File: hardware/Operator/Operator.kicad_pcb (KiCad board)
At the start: 2 copper layers, 53.8 x 54.2 mm, 11 parts, among them J1 RJ45, J2 Screw_Terminal_01x02, J3 Conn_01x06_Male, U1 DS89C21

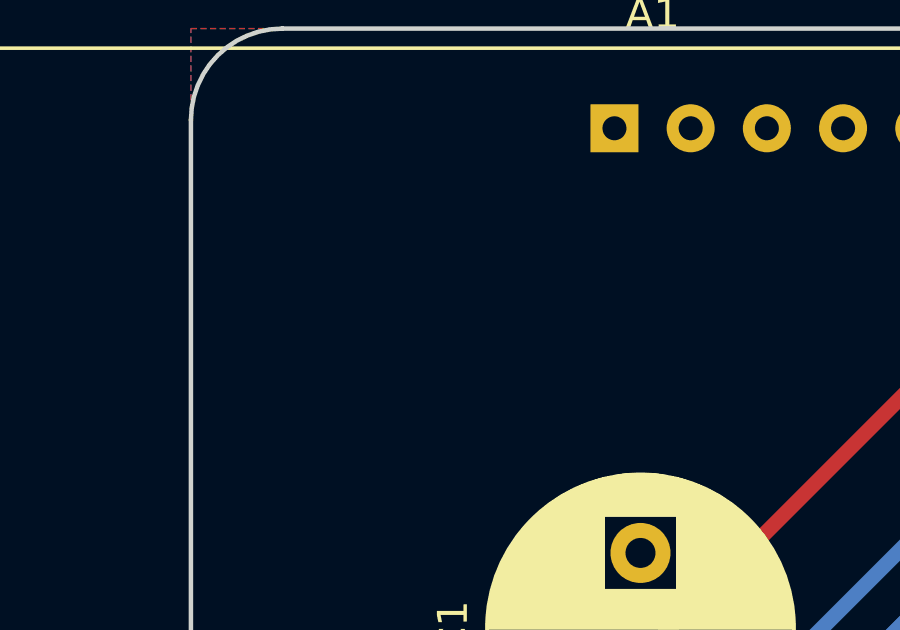
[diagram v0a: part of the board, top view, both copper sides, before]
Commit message: Created silk screen
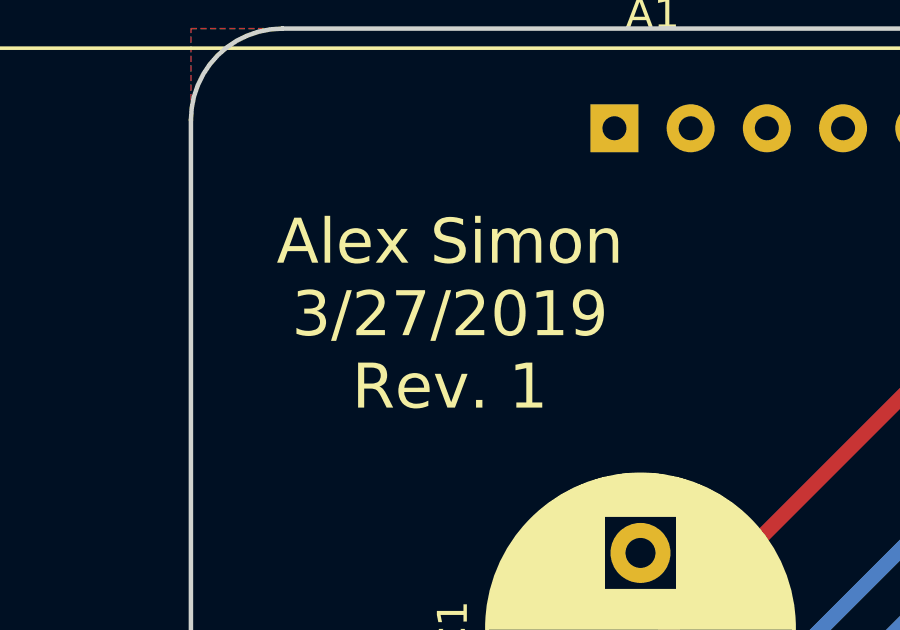
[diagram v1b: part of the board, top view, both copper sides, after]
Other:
- board text added: "Alex Simon 3/27/2019 Rev. 1"
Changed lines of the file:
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@@
   (general
     (thickness 1.6)
-    (drawings 8)
+    (drawings 9)
     (tracks 95)
     (zones 0)
@@
     )
   )
+  (gr_text "Alex Simon\n3/27/2019\nRev. 1" (at 141.986 59.817) (layer F.SilkS)
+    (effects (font (size 1.5 1.5) (thickness 0.3)))
+  )
   (gr_arc (start 184.15 53.34) (end 187.198 53.34) (angle -90) (layer Edge.Cuts) (width 0.15))

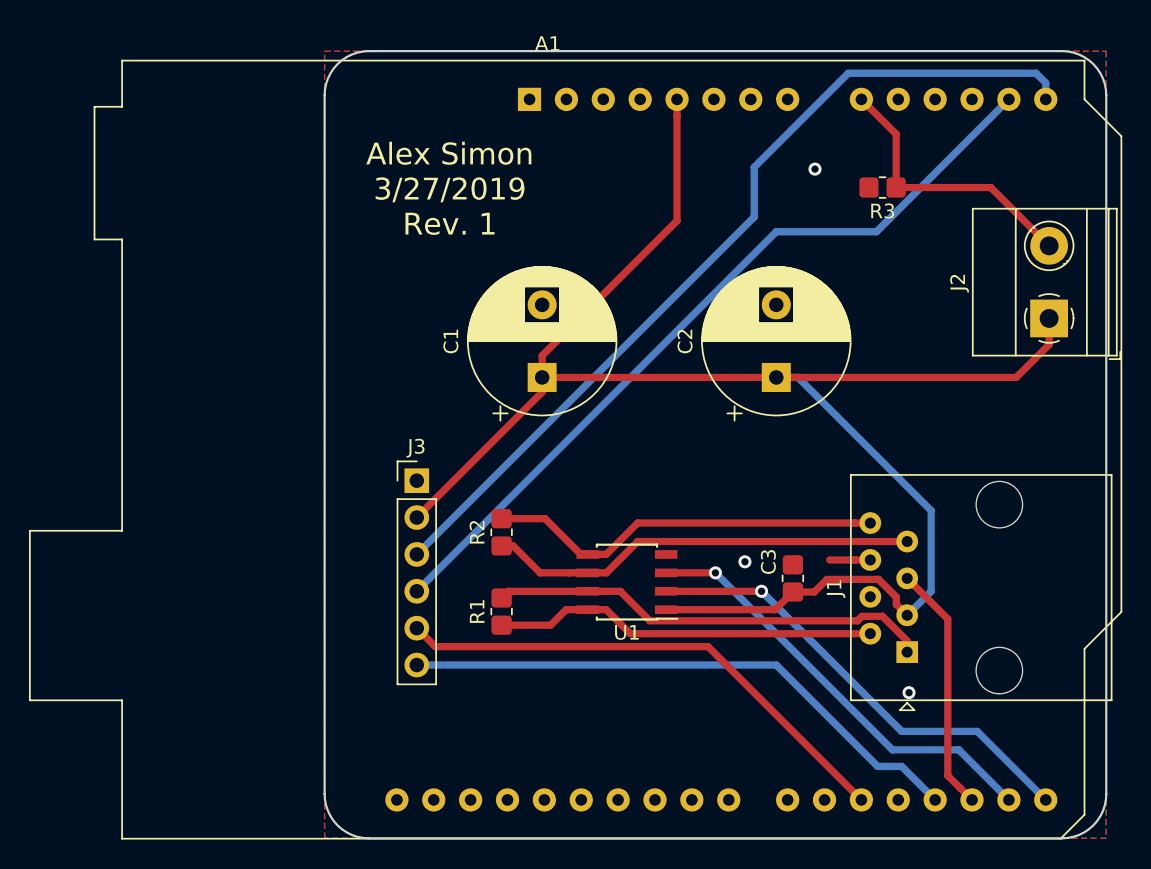
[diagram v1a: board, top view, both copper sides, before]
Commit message: Updated footprint size, put arduino on opposite side of board.
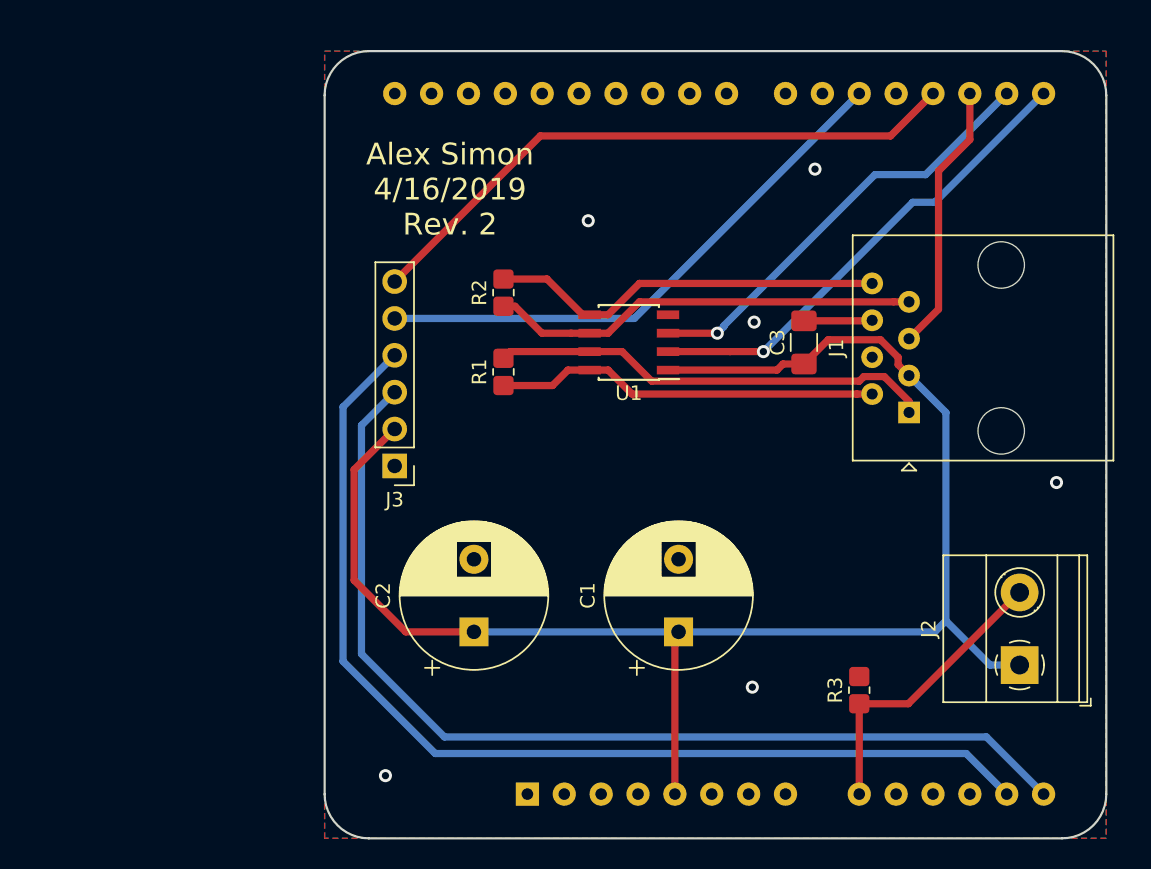
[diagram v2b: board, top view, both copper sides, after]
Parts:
- A1: moved to B.Cu
- C3: value 2.2nF -> 2.2uF; footprint Capacitor_SMD:C_0805_2012Metric_Pad1.33x1.40mm_HandSolder -> Capacitor_SMD:C_1206_3216Metric_Pad1.42x1.75mm_HandSolder
- moved A1 47.9 mm to (147.3, 101.5)
- moved R3 34.7 mm to (170.2, 94.3), turned to 90 degrees
- moved C2 27.2 mm to (143.6, 90.3)
- moved J2 24.0 mm to (181.2, 92.6)
- moved C1 19.9 mm to (157.7, 90.3)
- moved J1 16.5 mm to (173.6, 75.2)
- moved R1 16.5 mm to (145.7, 72.4)
- moved R2 16.5 mm to (145.7, 66.9)
- moved U1 16.5 mm to (154.3, 70.4)
- moved C3 16.3 mm to (166.4, 70.4)
- moved J3 1.83 mm to (138.2, 78.9), turned to 180 degrees
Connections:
- A1 pad 1: Net-(A1-Pad1) -> (no net)
- A1 pad 10: Net-(A1-Pad10) -> (no net)
- A1 pad 11: Net-(A1-Pad11) -> (no net)
- A1 pad 12: Net-(A1-Pad12) -> (no net)
- A1 pad 19: Net-(A1-Pad19) -> (no net)
- A1 pad 2: Net-(A1-Pad2) -> (no net)
- A1 pad 21: Net-(A1-Pad21) -> (no net)
- A1 pad 22: Net-(A1-Pad22) -> (no net)
- A1 pad 23: Net-(A1-Pad23) -> (no net)
- A1 pad 24: Net-(A1-Pad24) -> (no net)
- A1 pad 25: Net-(A1-Pad25) -> (no net)
- A1 pad 26: Net-(A1-Pad26) -> (no net)
- A1 pad 27: Net-(A1-Pad27) -> (no net)
- A1 pad 28: Net-(A1-Pad28) -> (no net)
- A1 pad 3: Net-(A1-Pad3) -> (no net)
- A1 pad 30: Net-(A1-Pad30) -> (no net)
- A1 pad 31: Net-(A1-Pad31) -> (no net)
- A1 pad 32: Net-(A1-Pad32) -> (no net)
- A1 pad 4: Net-(A1-Pad4) -> (no net)
- A1 pad 8: Net-(A1-Pad8) -> (no net)
- J1 pad 4: Net-(J1-Pad4) -> (no net)
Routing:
- net /A4: track 54.8 -> 72.1 mm
- net /A5: track 60.5 -> 70.0 mm
- net /5v: track 115.0 -> 108.5 mm
- net /D5: track 35.5 -> 38.4 mm
- net /D3: track 39.6 -> 42.4 mm
- net /GND: track 2.79 -> 4.71 mm, vias 3 -> 6
- net /TransEnable_TTL: track 17.1 -> 18.6 mm
- net /A0: track 19.3 -> 20.4 mm
- net /USART_RX: track 32.1 -> 33.2 mm
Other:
- board text added: "Alex Simon 4/16/2019 Rev. 2"
- board text removed: "Alex Simon 3/27/2019 Rev. 1"

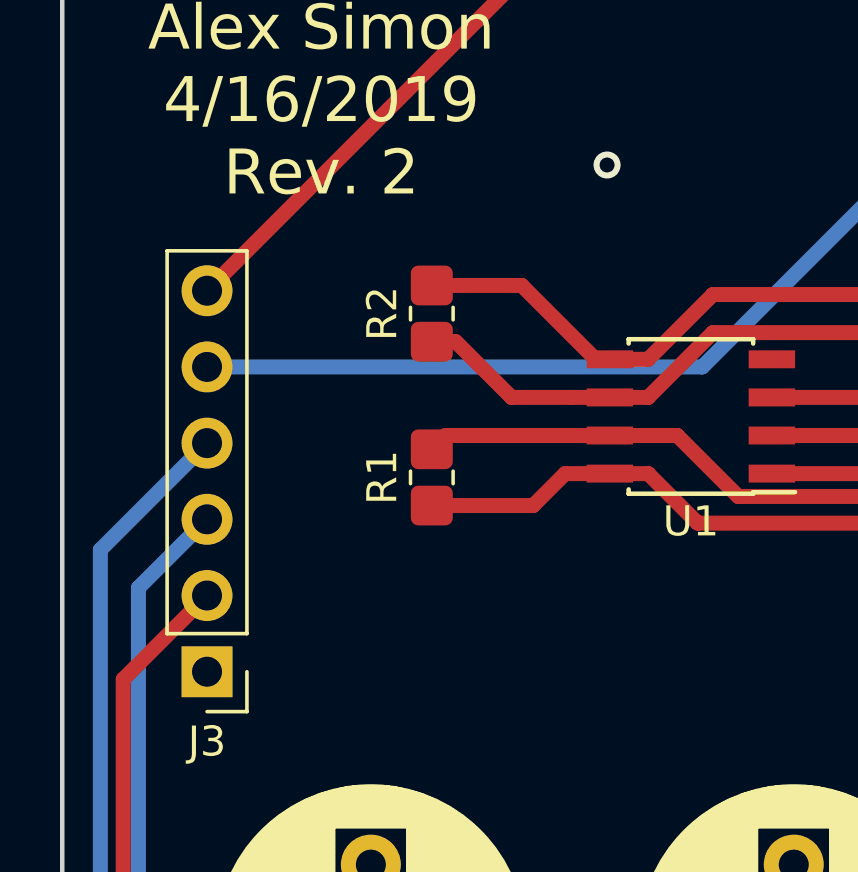
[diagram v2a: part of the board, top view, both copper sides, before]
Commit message: Added RS485 Bias resistors
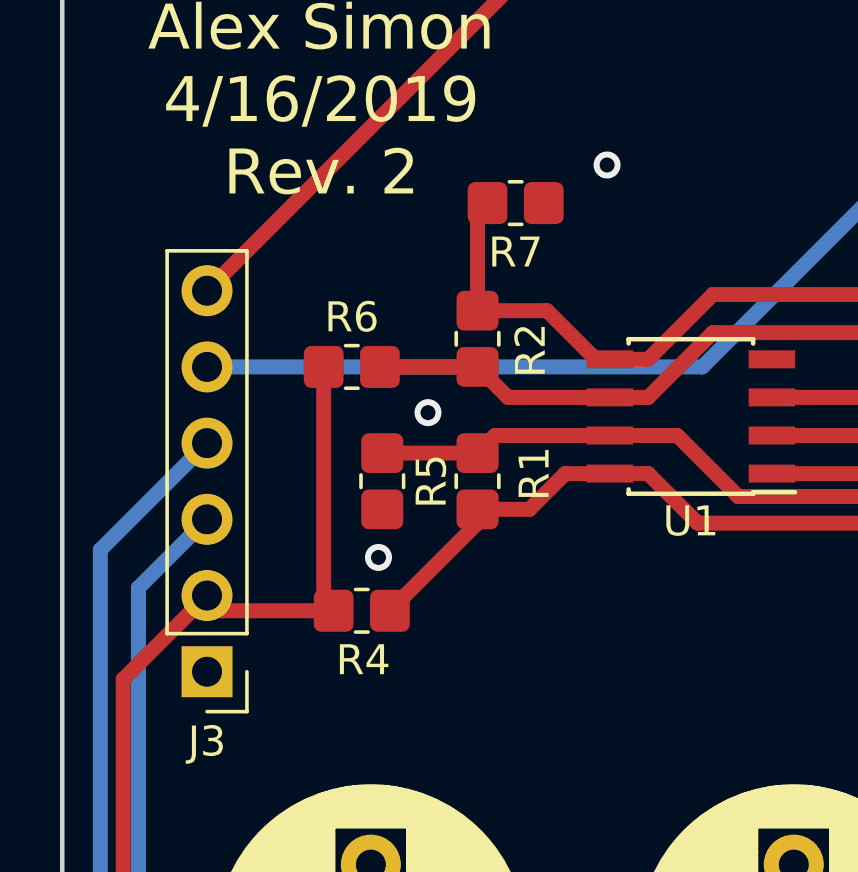
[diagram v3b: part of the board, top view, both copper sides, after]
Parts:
- added R4: 680, Resistor_SMD:R_0805_2012Metric_Pad1.33x1.40mm_HandSolder, F.Cu at (143.3, 76.8)
- added R5: 680, Resistor_SMD:R_0805_2012Metric_Pad1.33x1.40mm_HandSolder, F.Cu at (144.0, 72.5)
- added R6: 680, Resistor_SMD:R_0805_2012Metric_Pad1.33x1.40mm_HandSolder, F.Cu at (143.0, 68.7)
- added R7: 680, Resistor_SMD:R_0805_2012Metric_Pad1.33x1.40mm_HandSolder, F.Cu at (148.5, 63.2)
- moved R2 1.74 mm to (147.2, 67.8)
- moved R1 1.53 mm to (147.2, 72.5)
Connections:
- A1 pad 1: (no net) -> Net-(A1-Pad1)
- A1 pad 10: (no net) -> Net-(A1-Pad10)
- A1 pad 11: (no net) -> Net-(A1-Pad11)
- A1 pad 12: (no net) -> Net-(A1-Pad12)
- A1 pad 19: (no net) -> Net-(A1-Pad19)
- A1 pad 2: (no net) -> Net-(A1-Pad2)
- A1 pad 21: (no net) -> Net-(A1-Pad21)
- A1 pad 22: (no net) -> Net-(A1-Pad22)
- A1 pad 23: (no net) -> Net-(A1-Pad23)
- A1 pad 24: (no net) -> Net-(A1-Pad24)
- A1 pad 25: (no net) -> Net-(A1-Pad25)
- A1 pad 26: (no net) -> Net-(A1-Pad26)
- A1 pad 27: (no net) -> Net-(A1-Pad27)
- A1 pad 28: (no net) -> Net-(A1-Pad28)
- A1 pad 3: (no net) -> Net-(A1-Pad3)
- A1 pad 30: (no net) -> Net-(A1-Pad30)
- A1 pad 31: (no net) -> Net-(A1-Pad31)
- A1 pad 32: (no net) -> Net-(A1-Pad32)
- A1 pad 4: (no net) -> Net-(A1-Pad4)
- A1 pad 8: (no net) -> Net-(A1-Pad8)
- J1 pad 4: (no net) -> Net-(J1-Pad4)
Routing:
- net /5v: track 108.5 -> 121.2 mm
- net /+RX: track 26.5 -> 29.6 mm
- net /-TX: track 27.3 -> 29.2 mm
- net /-RX: track 30.6 -> 32.3 mm
- net /+Tx: track 29.6 -> 31.0 mm
- net /GND: vias 6 -> 8

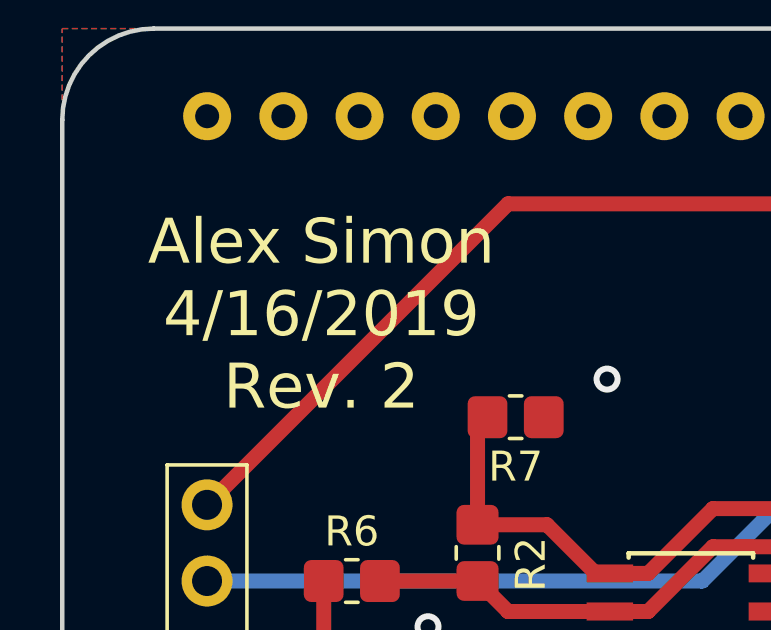
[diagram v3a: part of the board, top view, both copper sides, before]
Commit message: Updated silk screen
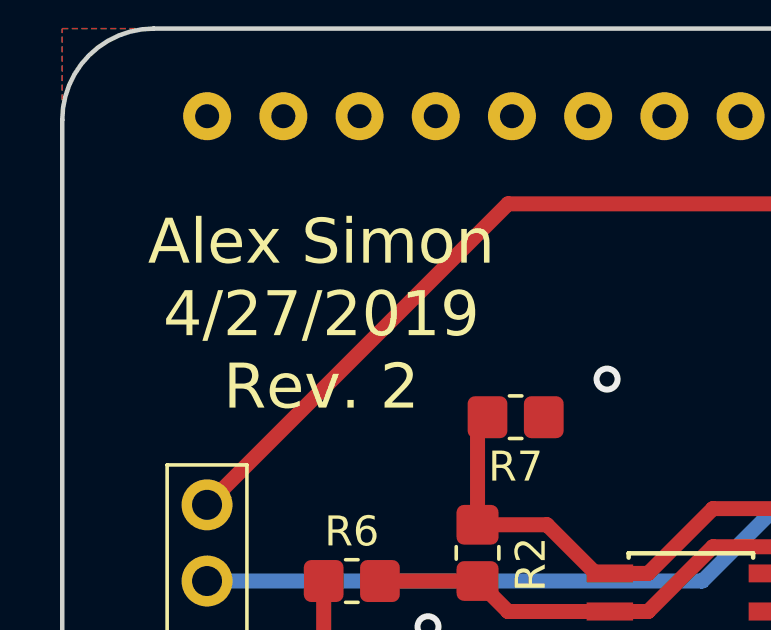
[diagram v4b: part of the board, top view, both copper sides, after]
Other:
- board text added: "Alex Simon 4/27/2019 Rev. 2"
- board text removed: "Alex Simon 4/16/2019 Rev. 2"
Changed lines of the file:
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@@
     )
   )
-  (gr_text "Alex Simon\n4/16/2019\nRev. 2" (at 141.986 59.817) (layer F.SilkS)
+  (gr_text "Alex Simon\n4/27/2019\nRev. 2" (at 141.986 59.817) (layer F.SilkS)
     (effects (font (size 1.5 1.5) (thickness 0.3)))
   )

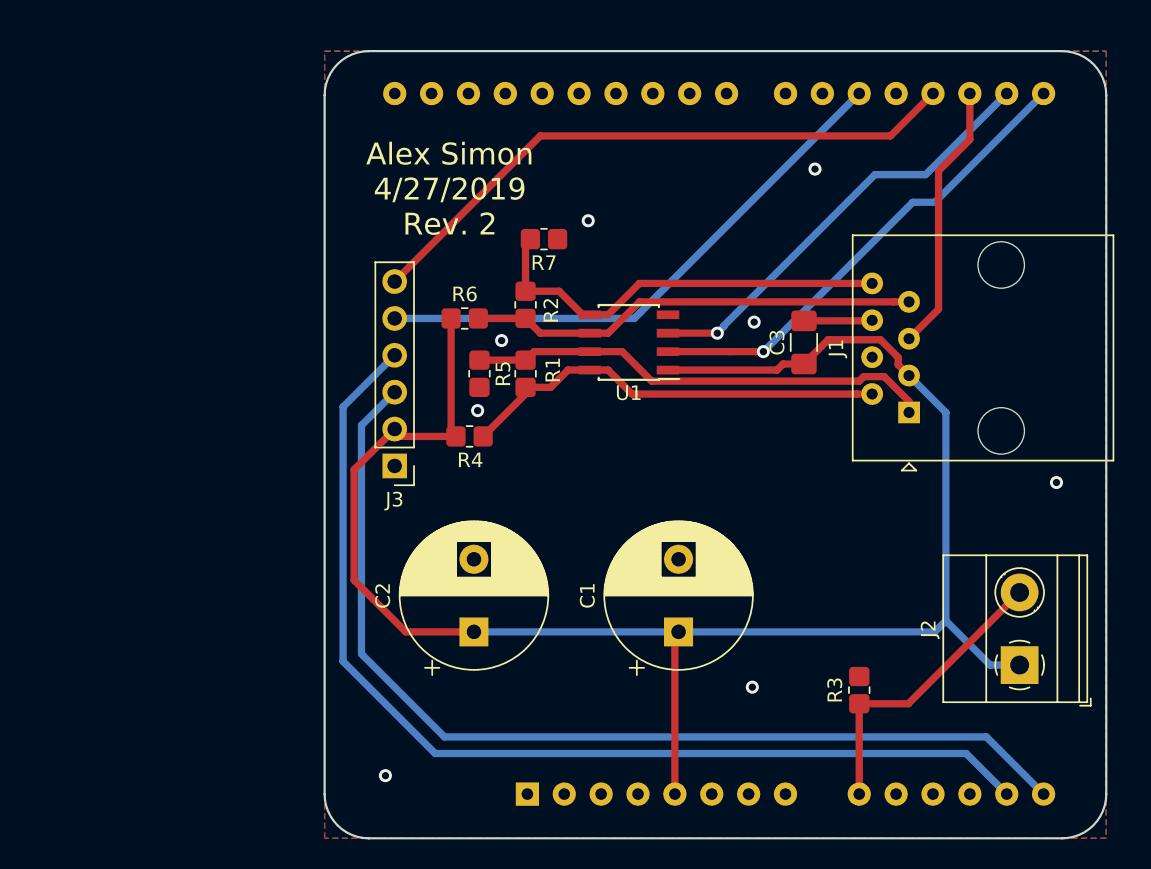
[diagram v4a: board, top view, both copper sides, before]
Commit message: Made arduino holes bigger
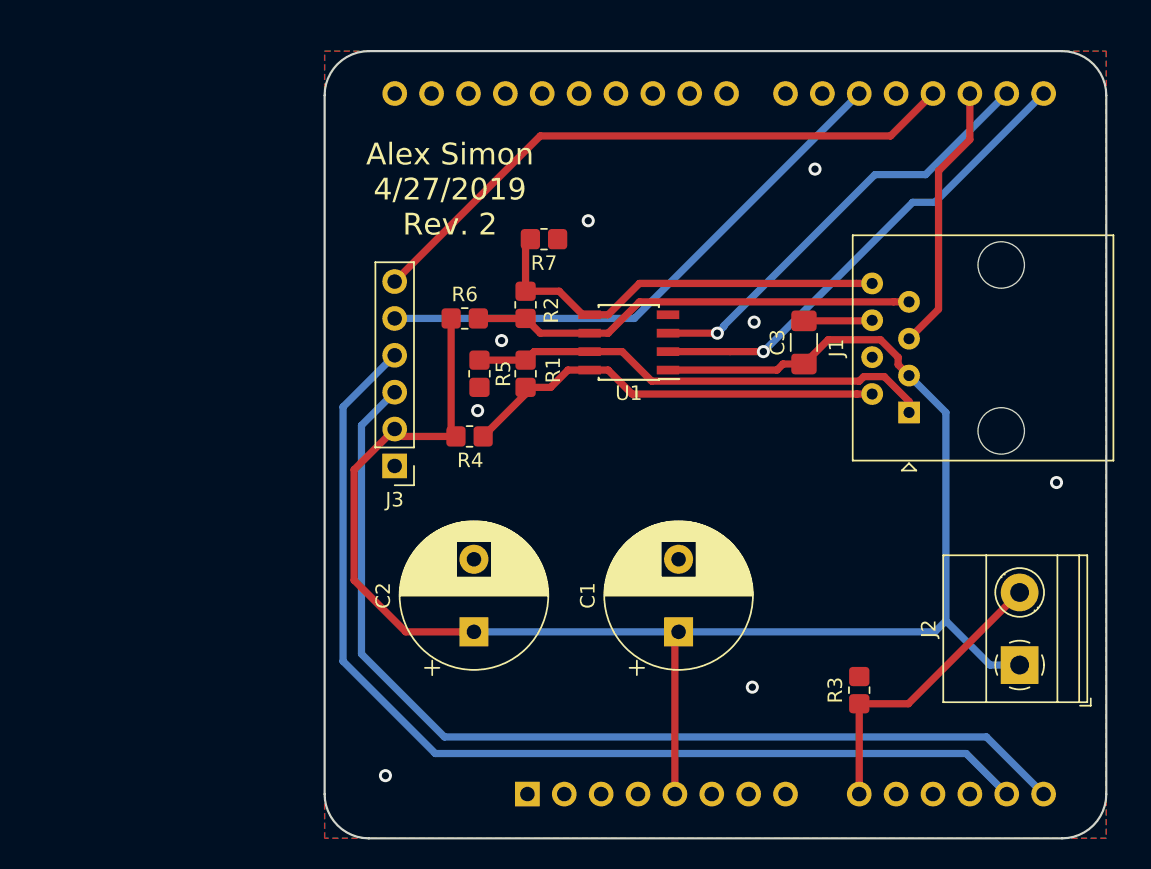
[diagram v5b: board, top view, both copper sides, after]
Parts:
- A1: footprint Module:Arduino_UNO_R3 -> Custom:Arduino_UNO_R3
